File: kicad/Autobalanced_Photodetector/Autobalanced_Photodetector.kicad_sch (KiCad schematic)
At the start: 0 parts

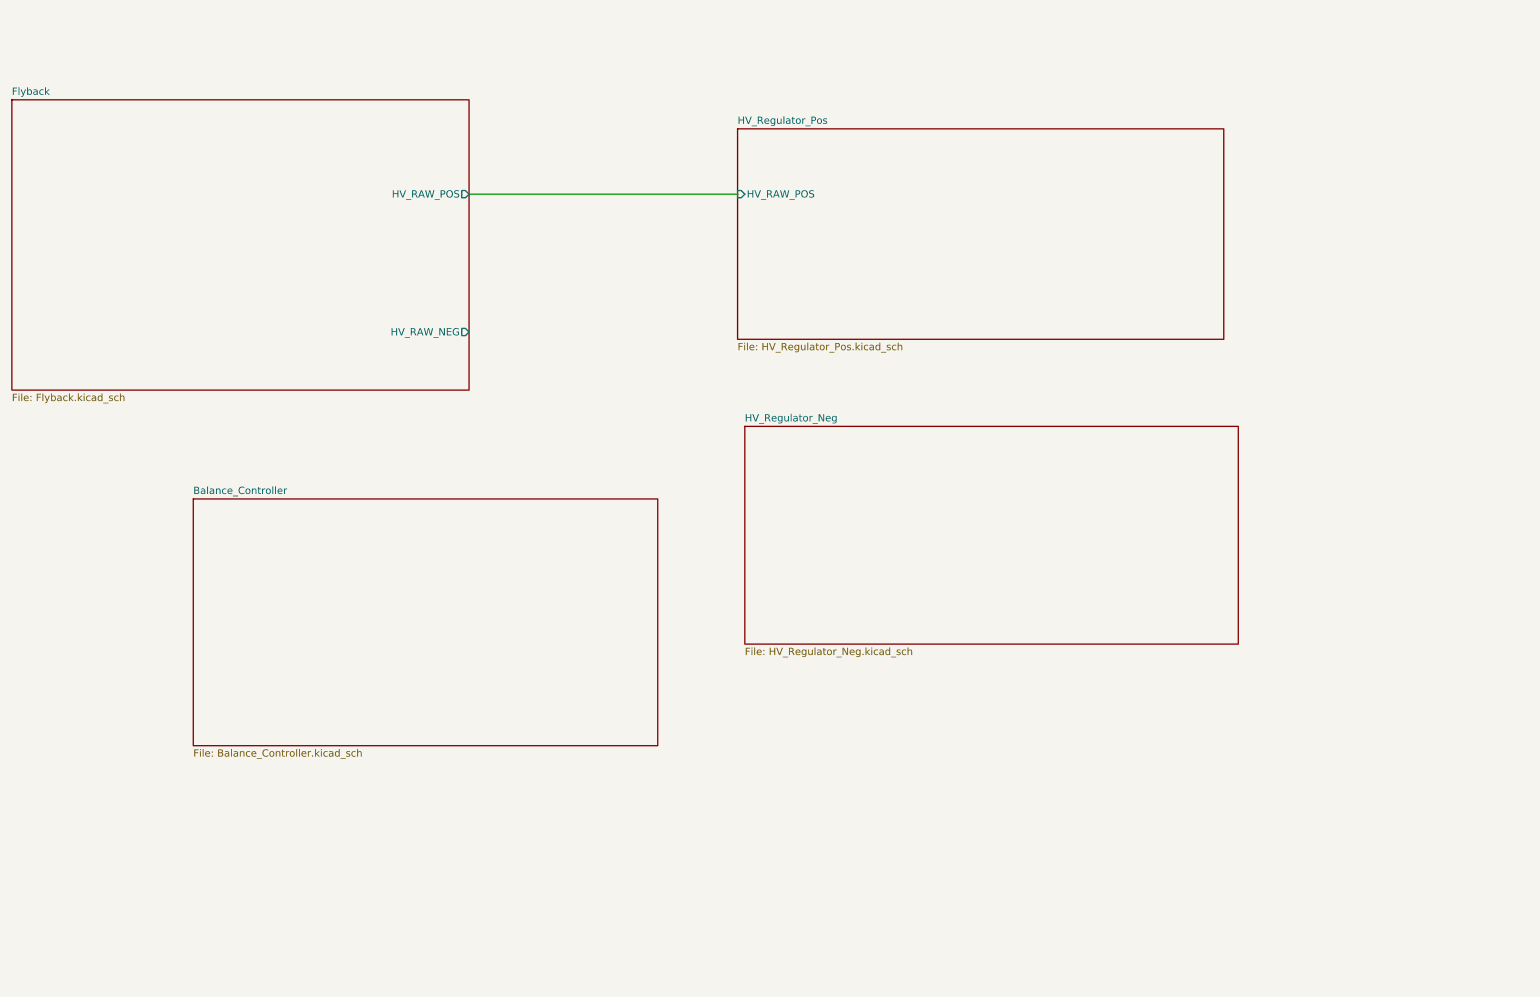
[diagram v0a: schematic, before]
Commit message: feat(kicad): add HV regulators and reference control
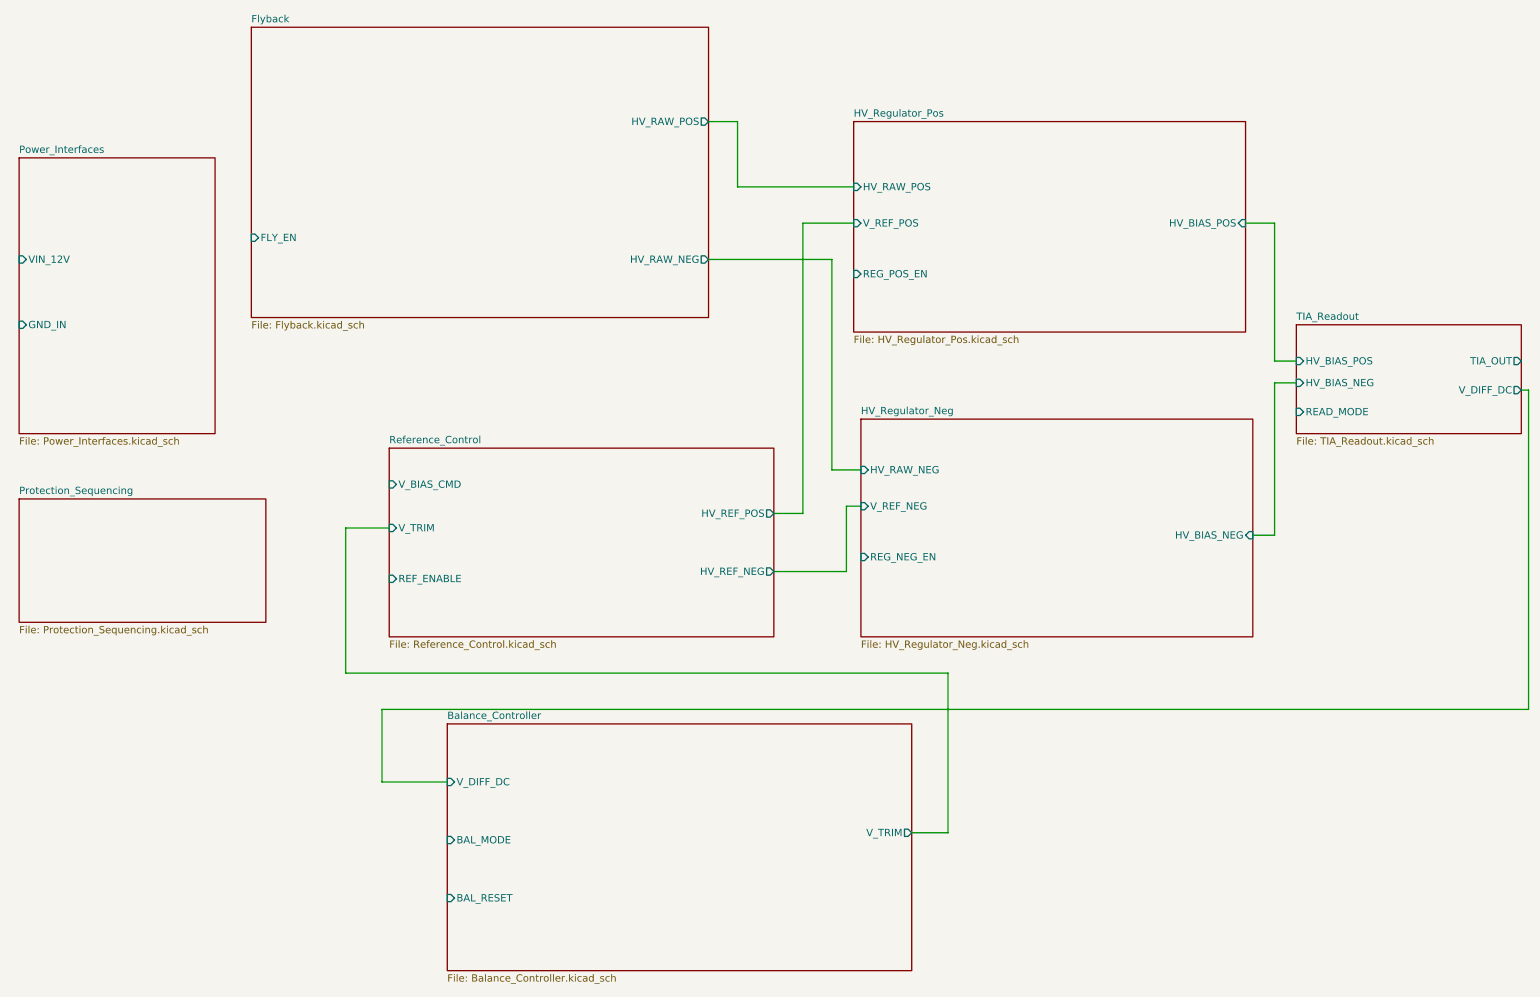
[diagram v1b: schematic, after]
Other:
- added sheet Power_Interfaces (Power_Interfaces.kicad_sch)
- added sheet Protection_Sequencing (Protection_Sequencing.kicad_sch)
- added sheet Reference_Control (Reference_Control.kicad_sch)
- added sheet TIA_Readout (TIA_Readout.kicad_sch)
- sheet Balance_Controller ports: added BAL_MODE, BAL_RESET, V_DIFF_DC, V_TRIM; removed none
- sheet Flyback ports: added FLY_EN; removed none
- sheet HV_Regulator_Neg ports: added HV_BIAS_NEG, HV_RAW_NEG, REG_NEG_EN, V_REF_NEG; removed none
- sheet HV_Regulator_Pos ports: added HV_BIAS_POS, REG_POS_EN, V_REF_POS; removed none
